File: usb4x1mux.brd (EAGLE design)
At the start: 123 x 80 mm, 44 parts, among them IC10 SN74LVC1G139DCTR, IC3 LDO5-3.3-SOT23, U1 LPC812M101JDH16

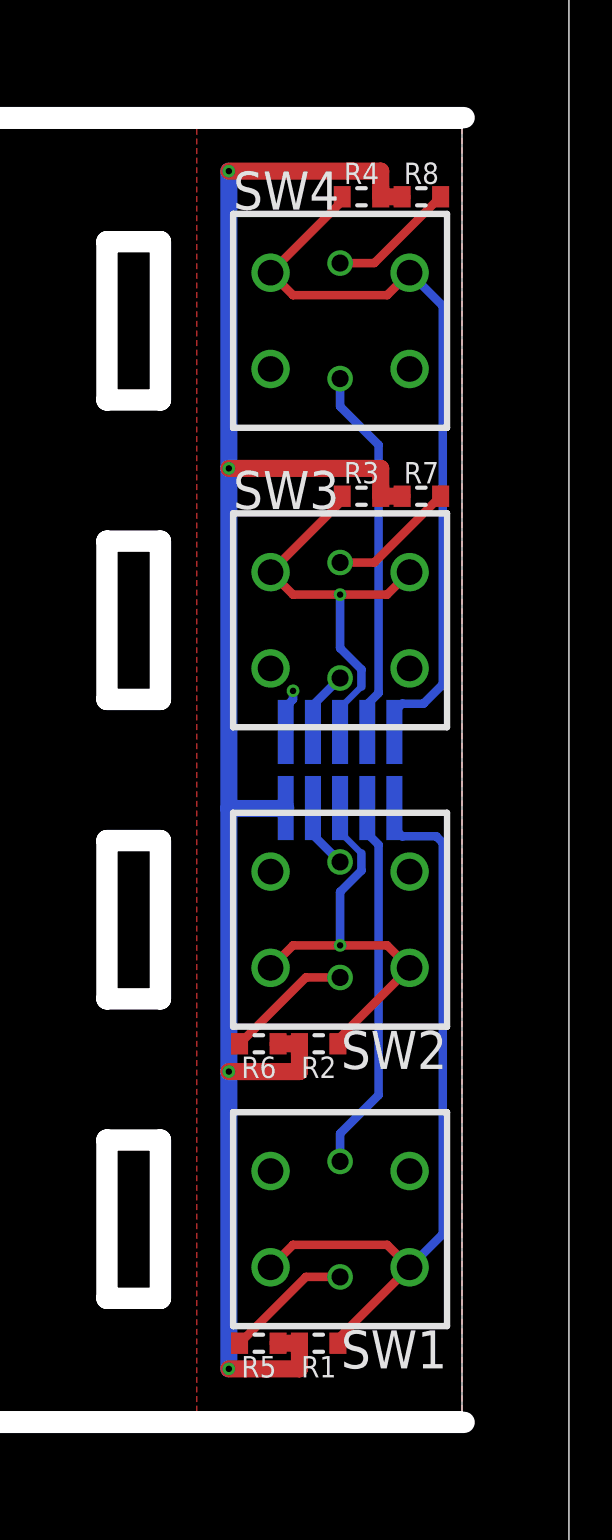
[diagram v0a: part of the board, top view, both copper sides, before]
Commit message: update hosts panel layout
it was keepout violation
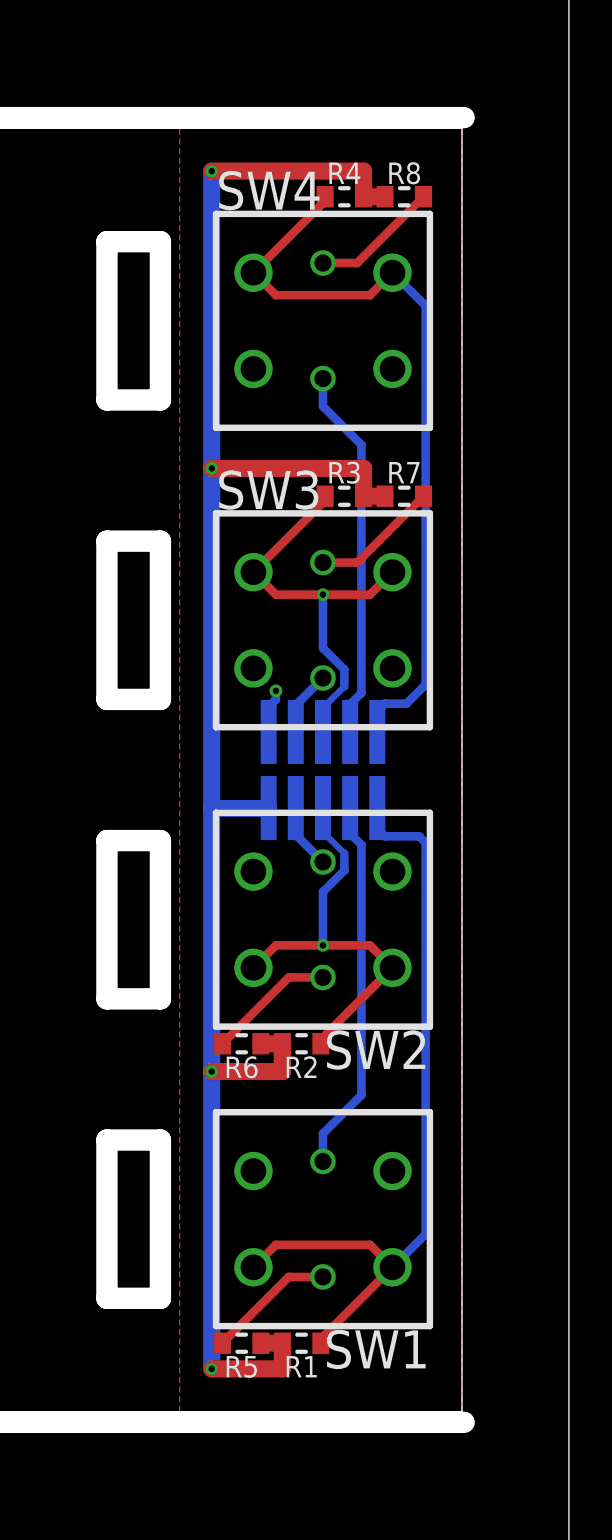
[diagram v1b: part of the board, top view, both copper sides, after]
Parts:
- moved CON7 0.80 mm to (111.5, 40.0)
- moved R1 0.80 mm to (110.5, 13.2)
- moved R2 0.80 mm to (110.5, 27.2)
- moved R3 0.80 mm to (112.5, 52.8)
- moved R4 0.80 mm to (112.5, 66.8)
- moved R5 0.80 mm to (107.7, 13.2)
- moved R6 0.80 mm to (107.7, 27.2)
- moved R7 0.80 mm to (115.3, 52.8)
- moved R8 0.80 mm to (115.3, 66.8)
- moved SW1 0.80 mm to (111.5, 19.0)
- moved SW2 0.80 mm to (111.5, 33.0)
- moved SW3 0.80 mm to (111.5, 47.0)
- moved SW4 0.80 mm to (111.5, 61.0)
